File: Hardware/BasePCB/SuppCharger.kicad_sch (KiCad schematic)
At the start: 10 parts, among them U1 TPS27SA08-Q1, U8 Supp Charger

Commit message: 0 unrouted nets :0 (all my footprints are mad at me)
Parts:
- added D21: LED, LED_SMD:LED_0603_1608Metric_Pad1.05x0.95mm_HandSolder, symbol Device:LED
- added R36: 120, Resistor_SMD:R_0603_1608Metric_Pad0.98x0.95mm_HandSolder, symbol Device:R
- TP9: footprint TestPoint:TestPoint_Pad_D2.5mm -> TestPoint:TestPoint_THTPad_D3.0mm_Drill1.5mm
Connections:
- net Chrg: now also U8.15 (LTC4011_Chrg); no longer U8.11 (LTC4011_Chrg)
- net Chrg_Buck_Fault: now also U8.13 (LTC4011_Flt); no longer U8.15 (LTC4011_Flt)
- net GND: now also D21.1 (K)
- net LoadSw_Rd: now also R36.1
- net Ready: now also U8.11 (LTC4011_Rdy); no longer U8.13 (LTC4011_Rdy)
- new net: D21.2 (A), R36.2
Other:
- moved on the sheet: R12, R17

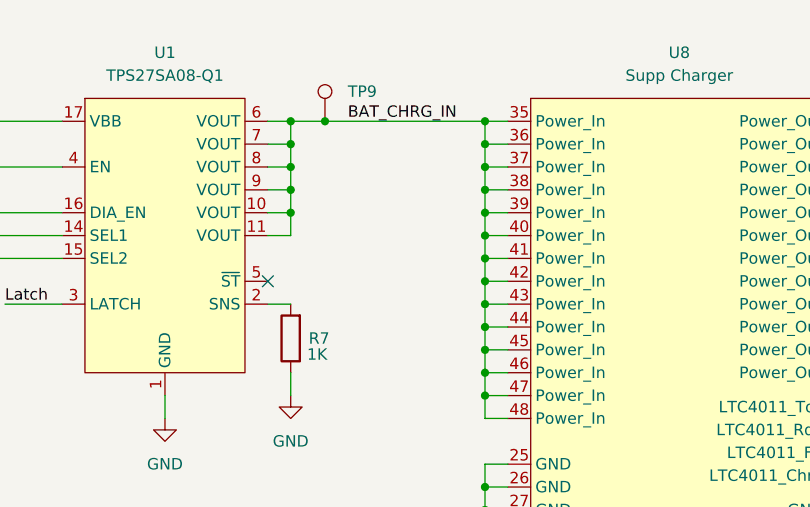
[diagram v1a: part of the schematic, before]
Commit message: add extra leds and sseg debug header
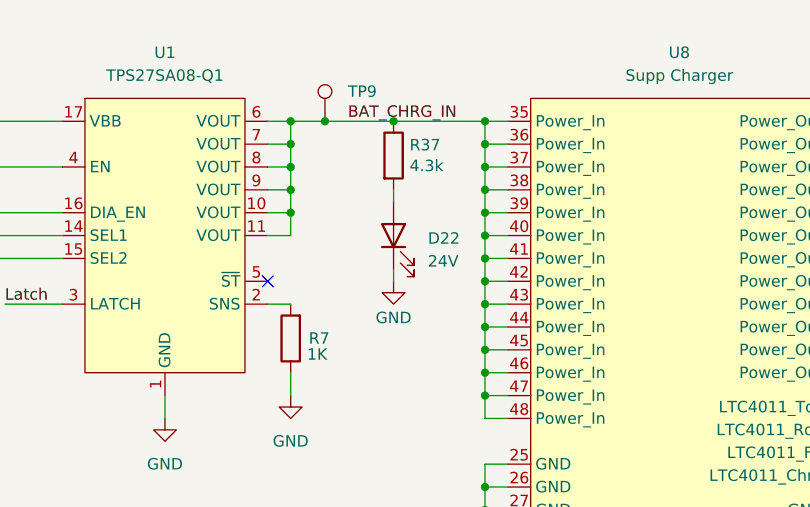
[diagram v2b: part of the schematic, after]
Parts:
- added D22: 24V, LED_SMD:LED_0603_1608Metric_Pad1.05x0.95mm_HandSolder, symbol Device:LED
- added R37: 4.3k, Resistor_SMD:R_0603_1608Metric_Pad0.98x0.95mm_HandSolder, symbol Device:R
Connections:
- net BAT_CHRG_IN: now also R37.1
- net GND: now also D22.1 (K)
- new net: D22.2 (A), R37.2

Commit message: BOM
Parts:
- TP9: now left out of the parts list
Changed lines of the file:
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@@
 		(unit 1)
 		(exclude_from_sim no)
-		(in_bom yes)
+		(in_bom no)
 		(on_board yes)
 		(dnp no)

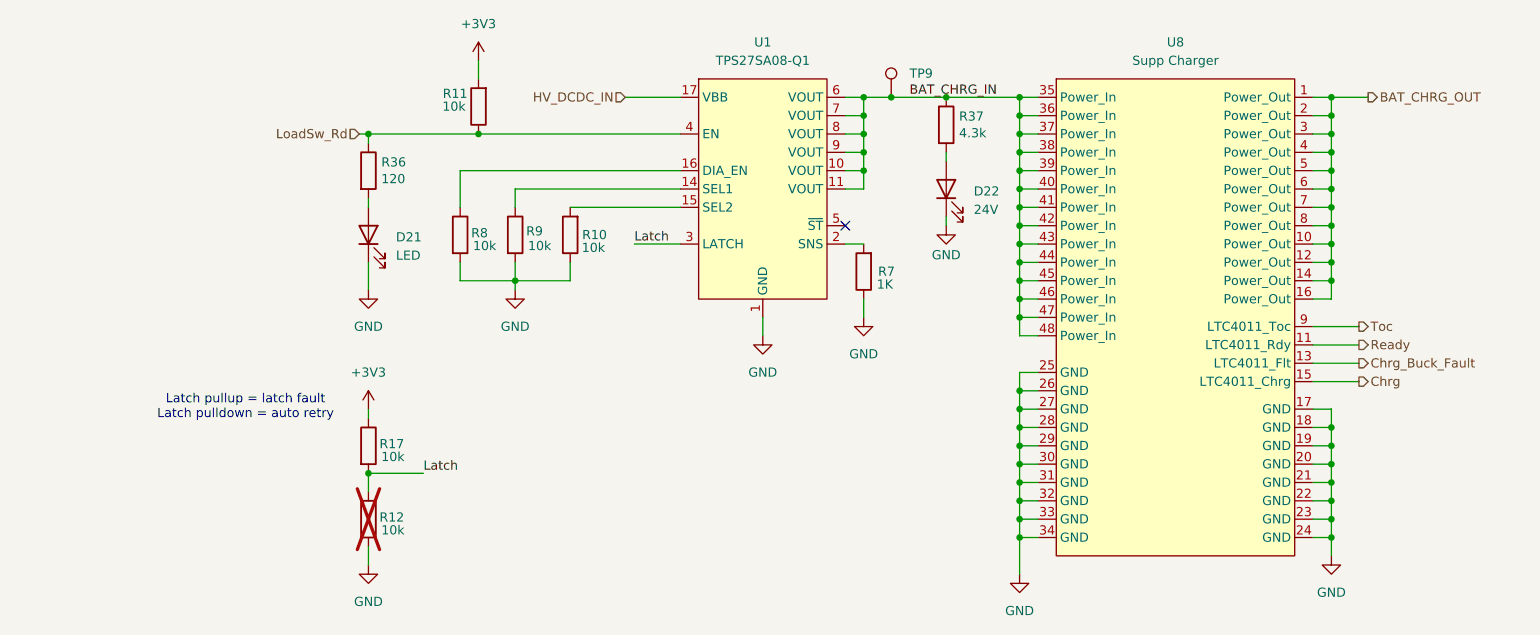
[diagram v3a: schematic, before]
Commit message: LV Base Rev B (#18)
* add hall effect sensor

* add LPF to ADC inputs

* schem done?

* supp charger routing done

* swap stat pins in supp charger

* cleanup a few stray traces

* supp bat hall effect routing

* adc lpf routing and layout

* only 4 traces left

* everything connected

* silk + panda

* minor silk changes

* align things

* add JLC p/n

* lil shah part 1

* new hall effect IC

* lil shah pt 2

* lil shah pt 3

* lil shah pt 3.5

* remove not needed kicad schematic sheet

* use kicad sharepoint NVFM symbol

* revert powermux changes accidentally pushed

* lv carrier jlc p/n

* changed supp charger to new footprint

* update lvmux 3d model

* add supp charger 3d model

* fck u lil shah

* rm numbers

---------

Co-authored-by: Frank Li <fxl77@my.utexas.edu>
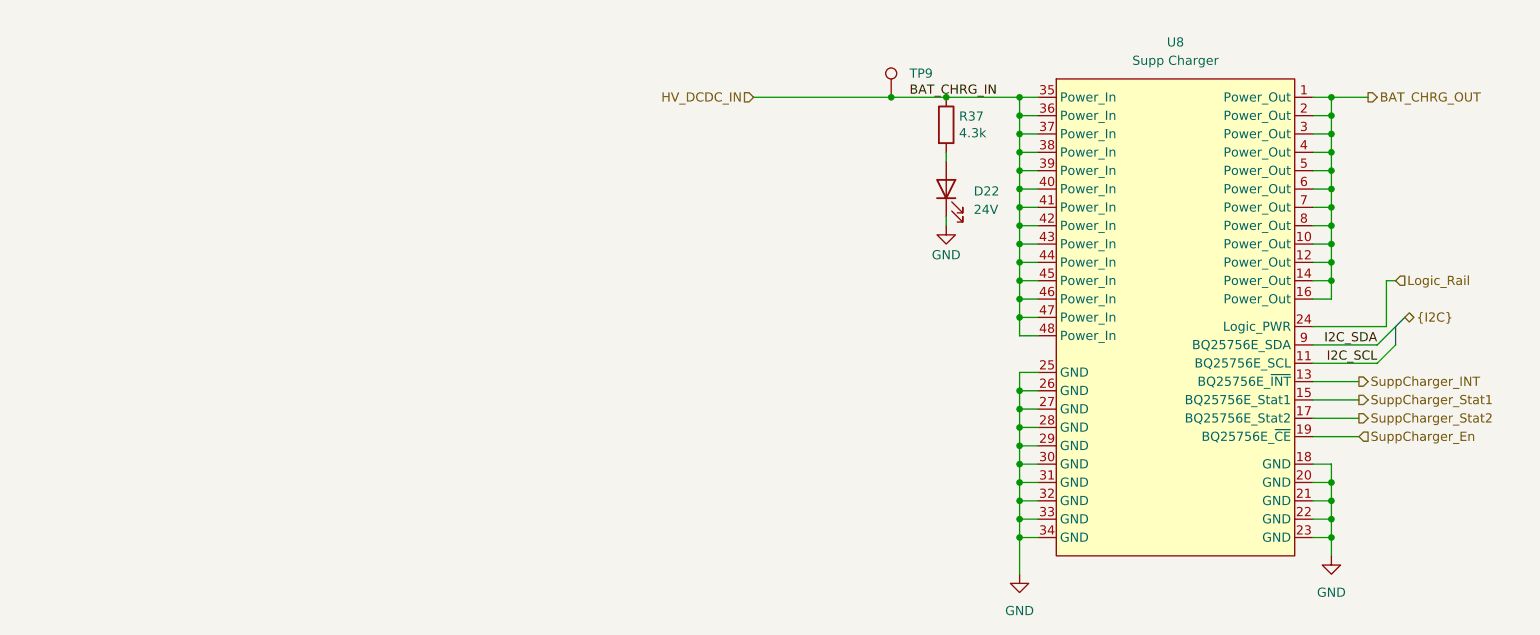
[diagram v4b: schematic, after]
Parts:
- removed D21: LED, LED_SMD:LED_0603_1608Metric_Pad1.05x0.95mm_HandSolder, symbol Device:LED
- removed R10, R11, R12, R17, R8, R9: 10k, Resistor_SMD:R_0603_1608Metric, symbol Device:R
- removed R36: 120, Resistor_SMD:R_0603_1608Metric_Pad0.98x0.95mm_HandSolder, symbol Device:R
- removed R7: 1K, Resistor_SMD:R_0603_1608Metric, symbol Device:R
- removed U1: TPS27SA08-Q1, Package_SO:HTSSOP-16-1EP_4.4x5mm_P0.65mm_EP3.4x5mm_Mask2.66x2.46mm_ThermalVias, symbol LV-Carrier:TPS27SA08-Q1
- D22: Assemble (none) -> Y; LSCS P/N (none) -> C7371904
- R37: Assemble (none) -> Y; LSCS P/N (none) -> C23162
- TP9, U8: Assemble (none) -> N
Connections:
- net BAT_CHRG_IN is gone; now on net HV_DCDC_IN: R37.1, TP9.1, U8.35 (Power_In), U8.36 (Power_In), U8.37 (Power_In), U8.38 (Power_In), U8.39 (Power_In), U8.40 (Power_In), U8.41 (Power_In), U8.42 (Power_In), U8.43 (Power_In), U8.44 (Power_In), U8.45 (Power_In), U8.46 (Power_In), U8.47 (Power_In), U8.48 (Power_In)
- net GND: no longer U8.17 (GND), U8.19 (GND), U8.24 (GND)
- net Chrg renamed SuppCharger_Stat1
- net Chrg_Buck_Fault renamed SuppCharger_INT
- net Ready renamed I2C_SCL
- net Toc renamed I2C_SDA
- new net Logic_Rail: U8.24 (Logic_PWR)
- new net SuppCharger_En: U8.19 (BQ25756E_~{CE})
- new net SuppCharger_Stat2: U8.17 (BQ25756E_Stat2)
- no-connect marks 1 -> 0
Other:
- note removed: "Latch pullup = latch fault Latch pulldown = auto retry"
